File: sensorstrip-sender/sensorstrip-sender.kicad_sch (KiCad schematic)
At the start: 11 parts, among them J1 USB_C_Receptacle_PowerOnly, J2 Conn_01x02_MountingPin, SW1 SW_DPDT_x2

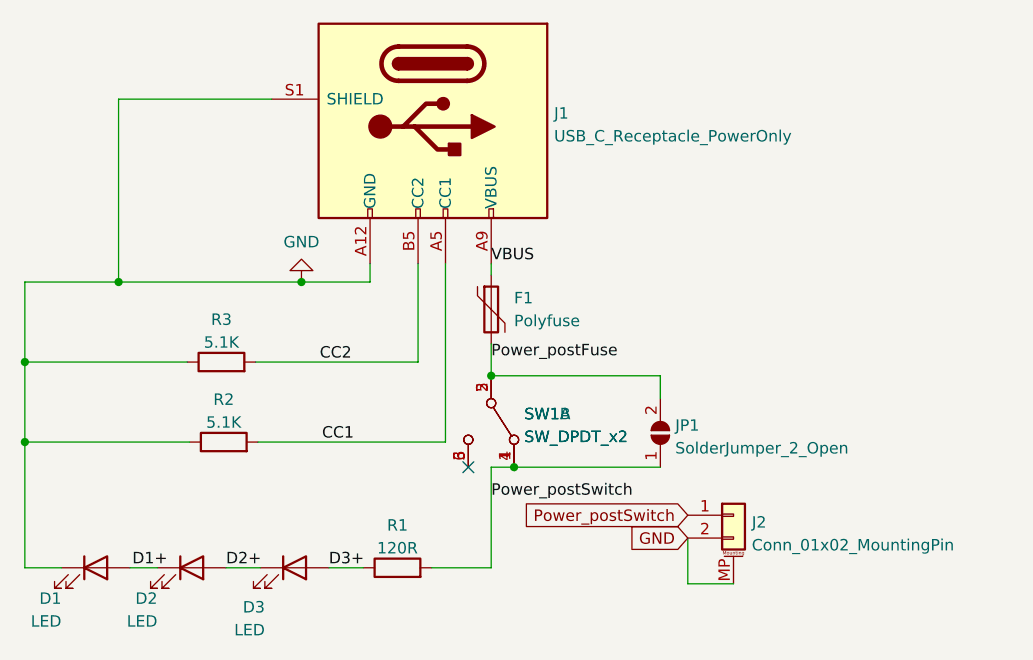
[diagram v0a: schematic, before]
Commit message: Cleanup in preparation for push
Update project files to KiCad 7 format
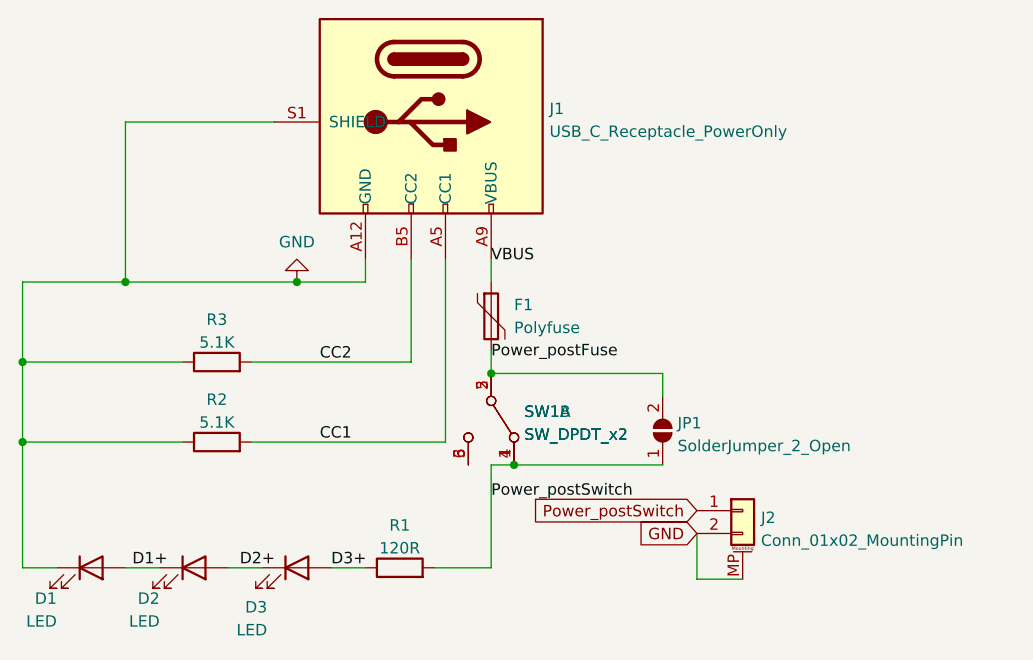
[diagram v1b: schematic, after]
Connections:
- no-connect marks 1 -> 0
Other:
- moved on the sheet: D1, F1, J1, J2, R2, R3

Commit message: Minor sensorstrip-sender revision:
- Swap PTH for NPTH
- Add through-holes to power switch pads for switch relocation
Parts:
- SW1: footprint sensorstrip:JS202011SCQN -> sensorstrip:JS202011SCQN-Hybrid
